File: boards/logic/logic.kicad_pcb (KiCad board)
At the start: 2 copper layers, 48.3 x 57.8 mm, 45 parts, among them IC1 ATTINY85-S, P1 5V_IN, P2 PROG_CONN, P3 DSPLY_CONN, Q1 Q_NPN_EBC, Q2 Q_NPN_EBC, Q3 Q_NPN_EBC, Q4 Q_NPN_EBC, Q5 Q_NPN_EBC, Q6 Q_NPN_EBC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

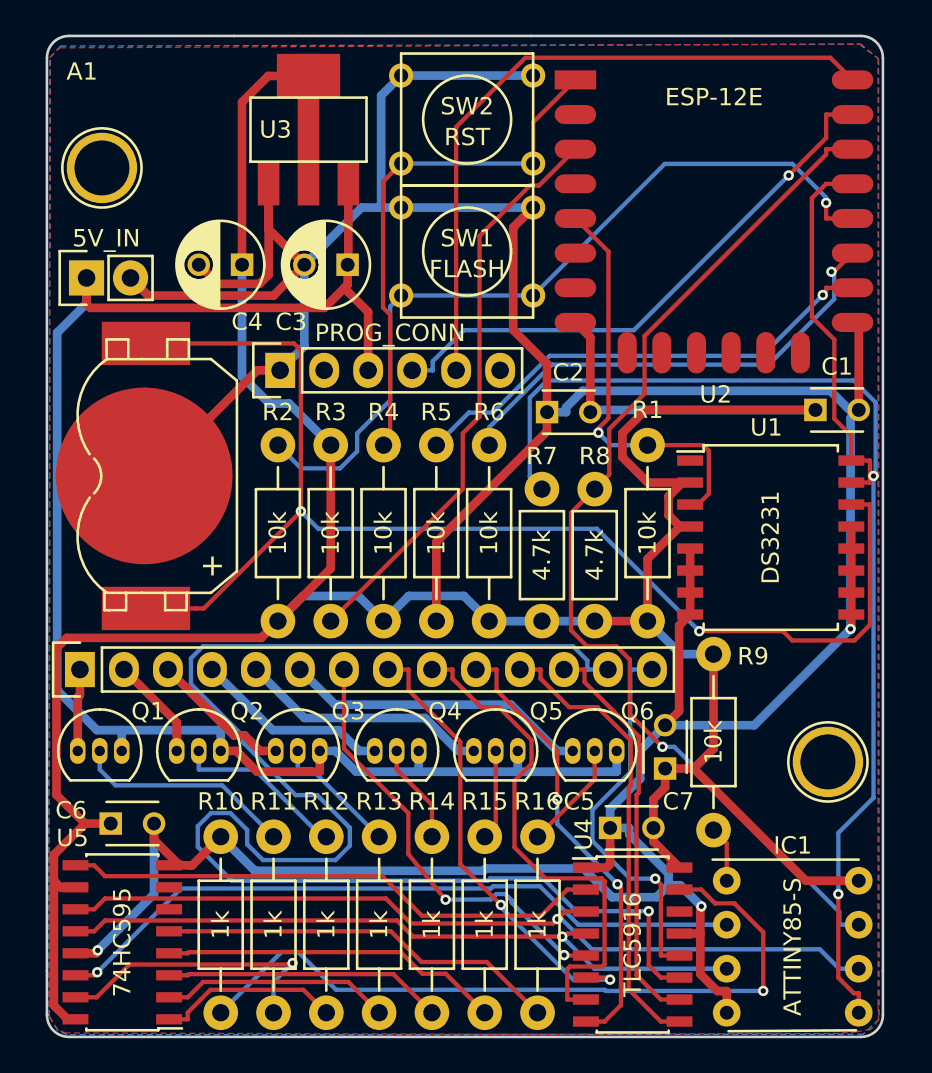
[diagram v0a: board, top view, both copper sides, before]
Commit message: Widened the board a tiny bit, and hand routed the majority of the display system.
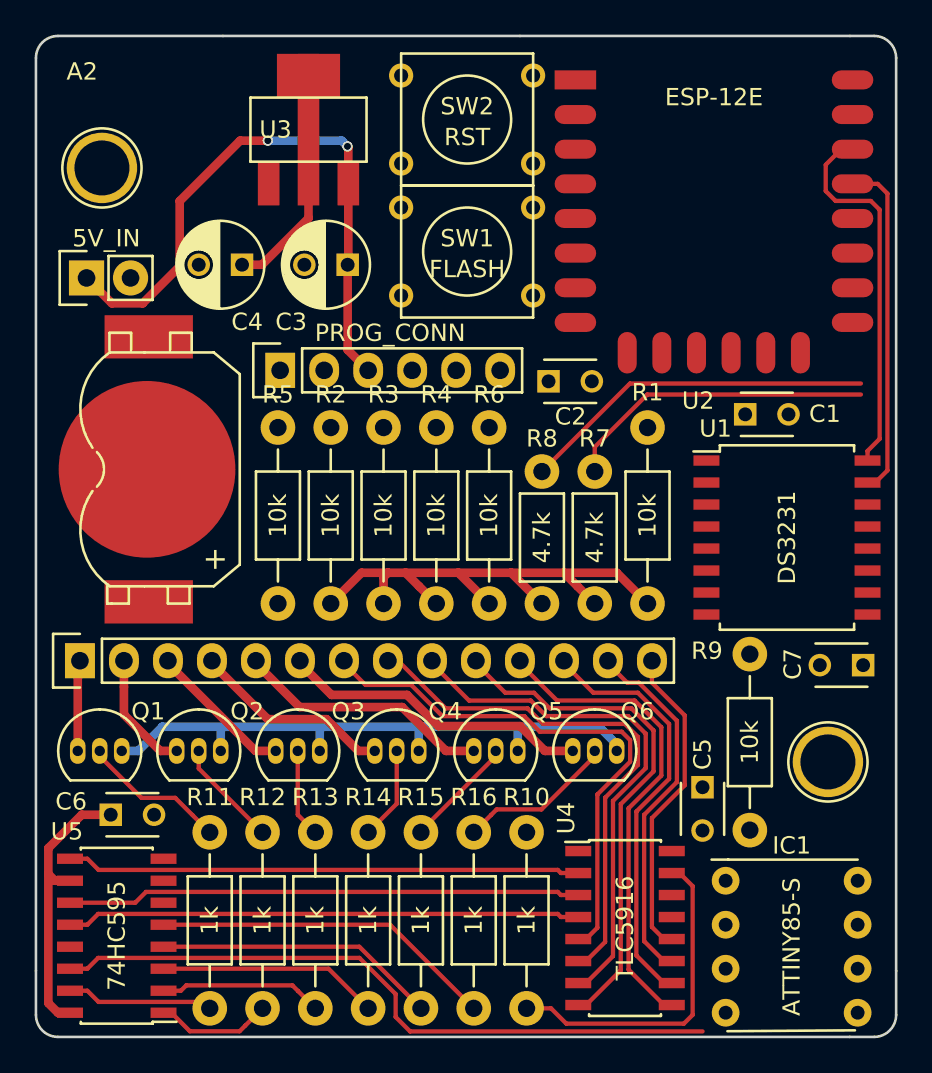
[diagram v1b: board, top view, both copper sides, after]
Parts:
- moved R10 17.7 mm to (149.0, 145.0)
- moved C7 12.9 mm to (168.4, 125.2), turned to 180 degrees
- moved R3 11.6 mm to (140.7, 111.5), turned to 270 degrees
- moved R5 9.20 mm to (134.6, 121.7)
- moved C5 5.83 mm to (159.1, 132.3), turned to 270 degrees
- moved C1 4.06 mm to (161.6, 110.7)
- moved R11 3.69 mm to (130.7, 134.9)
- moved R12 3.69 mm to (133.7, 134.9)
- moved R13 3.69 mm to (136.8, 134.9)
- moved R14 3.69 mm to (139.8, 134.9)
- moved R15 3.69 mm to (142.9, 134.9)
- moved R16 3.69 mm to (145.9, 134.9)
- moved R2 3.21 mm to (137.7, 121.7)
- moved R4 3.21 mm to (143.8, 121.7)
- moved R7 3.21 mm to (152.9, 121.7)
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- renumbered G*** to G1, G*** to G2
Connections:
- U1 pad 16: I2C_DATA -> I2C_CLCK
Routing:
- net GND: track 239.9 -> 0.00 mm, vias 3 -> 0
- net +3V3: track 184.9 -> 58.0 mm
- net Net-(BT1-Pad1): track 74.0 -> 0.00 mm, vias 2 -> 0
- net SEG_G: track 85.7 -> 21.2 mm, vias 1 -> 0
- net I2C_DATA: track 85.7 -> 37.7 mm, vias 2 -> 0
- net ESP_GPIO_0: track 46.8 -> 0.00 mm, vias 1 -> 0
- net CONN_RX: track 39.1 -> 0.00 mm
- net Net-(R3-Pad1): track 33.4 -> 0.00 mm
- net CONN_TX: track 32.6 -> 0.00 mm, vias 1 -> 0
- net ESP_RESET: track 30.5 -> 0.00 mm
- net Net-(R5-Pad2): track 27.9 -> 0.00 mm, vias 1 -> 0
- net Net-(R6-Pad2): track 27.3 -> 0.00 mm, vias 1 -> 0
- net ESP_GPIO_14: track 24.0 -> 0.00 mm, vias 1 -> 0
- net Net-(R10-Pad1): track 42.9 -> 19.1 mm, vias 1 -> 0
- net +5V: track 94.4 -> 71.7 mm, vias 0 -> 2
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- removed copper zone on B.Cu, net GND
- removed copper zone on F.Cu, net GND
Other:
- board size 48.3 x 57.8 mm -> 49.7 x 57.8 mm
- board text added: "A2"
- board text removed: "A1"

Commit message: Finished hand routing the board except for ground.
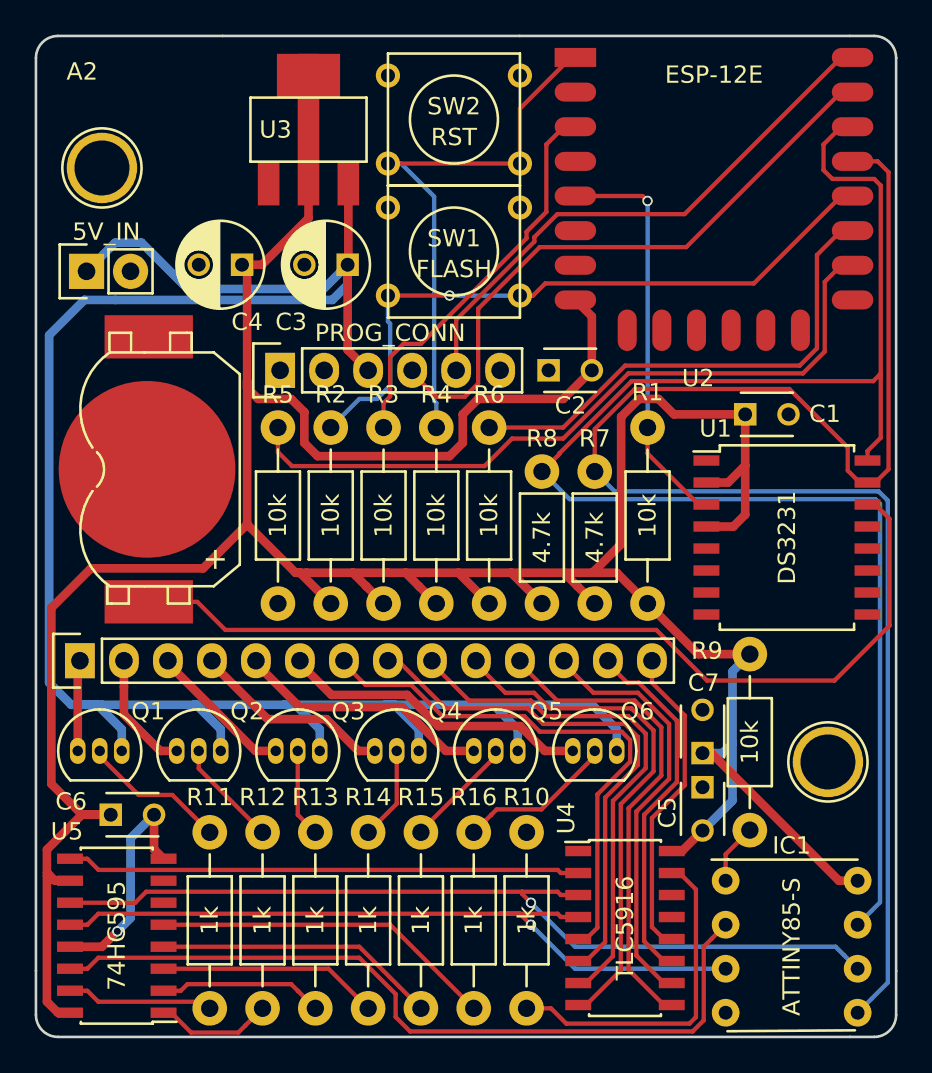
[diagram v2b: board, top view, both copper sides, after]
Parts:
- moved C7 10.6 mm to (159.1, 130.3), turned to 90 degrees
- moved U2 1.30 mm to (151.8, 90.1)
- moved SW1 0.76 mm to (144.8, 101.3)
- moved SW2 0.76 mm to (144.8, 93.7)
- moved C2 0.64 mm to (150.2, 108.2)
- moved P1 0.38 mm to (123.6, 102.5)
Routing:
- net +3V3: track 58.0 -> 203.8 mm
- net Net-(BT1-Pad1): track 0.00 -> 53.7 mm
- net I2C_DATA: track 37.7 -> 91.1 mm
- net +5V: track 71.7 -> 124.7 mm, vias 2 -> 0
- net I2C_CLCK: track 42.3 -> 90.4 mm
- net Net-(R5-Pad2): track 0.00 -> 42.1 mm
- net ESP_GPIO_0: track 0.00 -> 38.9 mm, vias 0 -> 1
- net CONN_TX: track 0.00 -> 36.0 mm
- net CONN_RX: track 0.00 -> 32.2 mm
- net ESP_RESET: track 0.00 -> 32.1 mm
- net Net-(R6-Pad2): track 0.00 -> 28.8 mm
- net ESP_GPIO_14: track 0.00 -> 23.5 mm, vias 0 -> 1
- net Net-(R3-Pad1): track 0.00 -> 22.9 mm
- net DISPLAY_SERIAL_CLOCK: track 29.7 -> 51.0 mm, vias 0 -> 1
- net DISPLAY_SERIAL_LATCH: track 29.7 -> 44.0 mm, vias 0 -> 1
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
